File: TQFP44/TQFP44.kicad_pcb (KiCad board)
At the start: 2 copper layers, 56.1 x 20.6 mm, 12 parts, among them J1 Conn_01x22, J2 Conn_01x22, J3 Conn_02x22_Counter_Clockwise, J4 Conn_02x22_Counter_Clockwise, J5 Conn_02x22_Counter_Clockwise, J6 Conn_01x06

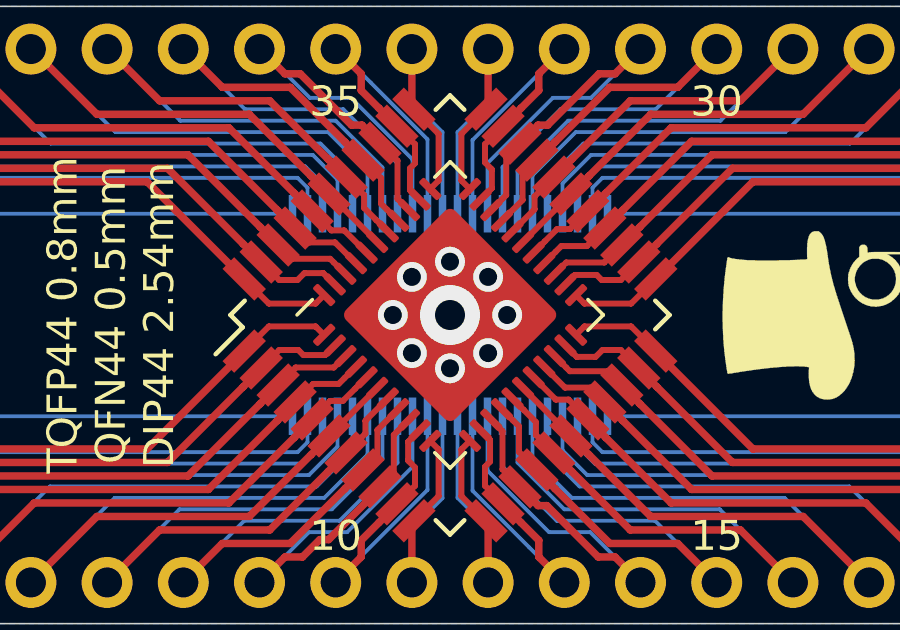
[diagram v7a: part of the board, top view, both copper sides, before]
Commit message: Silkscreen Edits
Dimensions moved to Drawings Layer
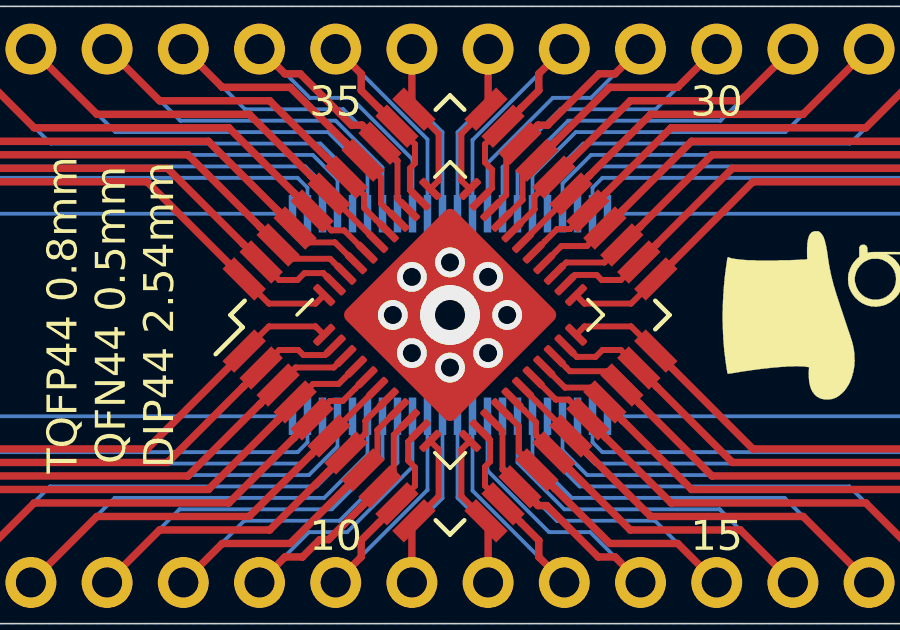
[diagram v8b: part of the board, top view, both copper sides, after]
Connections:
- J4 pad 45: (no net) -> Net-(J6-Pad1)
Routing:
- net Net-(J6-Pad1): vias 0 -> 9
- net (no net): vias 9 -> 0
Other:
- rule pad_to_mask_clearance: 0.051 -> 0
- rule solder_mask_min_width: 0.25 -> 0.1
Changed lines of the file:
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@@
   (page A4)
   (layers
-    (0 F.Cu signal)
+    (0 F.Cu signal hide)
     (31 B.Cu signal)
     (32 B.Adhes user hide)
@@
     (34 B.Paste user hide)
     (35 F.Paste user hide)
-    (36 B.SilkS user)
+    (36 B.SilkS user hide)
     (37 F.SilkS user)
     (38 B.Mask user)
-    (39 F.Mask user)
+    (39 F.Mask user hide)
     (40 Dwgs.User user)
     (41 Cmts.User user hide)
@@
     (pad_size 1.7 1.7)
     (pad_drill 1)
-    (pad_to_mask_clearance 0.051)
-    (solder_mask_min_width 0.25)
+    (pad_to_mask_clearance 0)
+    (solder_mask_min_width 0.1)
     (aux_axis_origin 0 0)
     (visible_elements 7FFFFFFF)
@@
       (usegerberadvancedattributes false)
       (creategerberjobfile false)
-      (excludeedgelayer false)
+      (excludeedgelayer true)
       (linewidth 0.100000)
       (plotframeref false)
       (viasonmask false)
       (mode 1)
-      (useauxorigin false)
+      (useauxorigin true)
       (hpglpennumber 1)
       (hpglpenspeed 20)
@@
     (pad "" smd roundrect (at -1.935 -0.645 45) (size 1.04 1.04) (layers F.Paste) (roundrect_rratio 0.240385))
     (pad "" smd roundrect (at -1.935 -1.935 45) (size 1.04 1.04) (layers F.Paste) (roundrect_rratio 0.240385))
-    (pad 45 smd roundrect (at 0 0 45) (size 5.15 5.15) (layers F.Cu F.Mask) (roundrect_rratio 0.048544))
+    (pad 45 smd roundrect (at 0 0 45) (size 5.15 5.15) (layers F.Cu F.Mask) (roundrect_rratio 0.048544)
+      (net 45 "Net-(J6-Pad1)"))
     (model ${KISYS3DMOD}/Package_DFN_QFN.3dshapes/QFN-44-1EP_7x7mm_P0.5mm_EP5.15x5.15mm.wrl
       (at (xyz 0 0 0))
@@
     (effects (font (size 1 1) (thickness 0.15)) (justify mirror))
   )
-  (dimension 56.134 (width 0.15) (layer F.SilkS)
-    (gr_text "56.134 mm" (at 194.437 56.0278) (layer F.SilkS)
+  (dimension 56.134 (width 0.15) (layer Dwgs.User)
+    (gr_text "56.134 mm" (at 194.437 56.0278) (layer Dwgs.User)
       (effects (font (size 1 1) (thickness 0.15)) hide)
     )
@@
     (arrow2b (pts (xy 166.37 57.3278) (xy 167.496504 56.741379)))
   )
-  (dimension 20.574 (width 0.15) (layer F.SilkS)
-    (gr_text "20.574 mm" (at 160.447298 72.39 270) (layer F.SilkS)
+  (dimension 20.574 (width 0.15) (layer Dwgs.User)
+    (gr_text "20.574 mm" (at 160.447298 72.39 270) (layer Dwgs.User)
       (effects (font (size 1 1) (thickness 0.15)) hide)
     )
@@
     (arrow2b (pts (xy 161.747298 62.103) (xy 162.333719 63.229504)))
   )
-  (dimension 17.78 (width 0.15) (layer F.SilkS)
-    (gr_text "17.780 mm" (at 163.5206 72.4154 270) (layer F.SilkS)
+  (dimension 17.78 (width 0.15) (layer Dwgs.User)
+    (gr_text "17.780 mm" (at 163.5206 72.4154 270) (layer Dwgs.User)
       (effects (font (size 1 1) (thickness 0.15)) hide)
     )
@@
     (arrow2b (pts (xy 164.8206 63.5254) (xy 165.407021 64.651904)))
   )
-  (dimension 53.34 (width 0.15) (layer F.SilkS)
-    (gr_text "53.340 mm" (at 194.437 58.7202) (layer F.SilkS)
+  (dimension 53.34 (width 0.15) (layer Dwgs.User)
+    (gr_text "53.340 mm" (at 194.437 58.7202) (layer Dwgs.User)
       (effects (font (size 1 1) (thickness 0.15)) hide)
     )
@@
   (gr_circle (center 195.707 73.66) (end 196.107 73.66) (layer F.Mask) (width 0.2))
   (gr_circle (center 195.715 73.66) (end 196.115 73.66) (layer B.Mask) (width 0.2))
-  (gr_circle (center 194.437 74.187) (end 194.837 74.187) (layer B.Mask) (width 0.2))
+  (gr_circle (center 194.437 74.149) (end 194.837 74.149) (layer B.Mask) (width 0.2))
   (gr_circle (center 194.437 74.168) (end 194.837 74.168) (layer F.Mask) (width 0.2))
   (gr_circle (center 193.175 73.66) (end 193.575 73.66) (layer B.Mask) (width 0.2))
@@
   (gr_line (start 166.37 63.5) (end 166.37 81.28) (layer Edge.Cuts) (width 0.05))
   (gr_line (start 221.107 62.103) (end 167.767 62.103) (layer Edge.Cuts) (width 0.05))
+  (via (at 194.437 72.39) (size 2) (drill 1) (layers F.Cu B.Cu) (net 45))
+  (via (at 192.532 72.39) (size 1) (drill 0.6) (layers F.Cu B.Cu) (net 45))
+  (via (at 196.342 72.39) (size 1) (drill 0.6) (layers F.Cu B.Cu) (net 45))
+  (via (at 194.437 70.6374) (size 1) (drill 0.6) (layers F.Cu B.Cu) (net 45))
+  (via (at 193.167 71.12) (size 1) (drill 0.6) (layers F.Cu B.Cu) (net 45))
+  (via (at 195.707 71.12) (size 1) (drill 0.6) (layers F.Cu B.Cu) (net 45))
+  (via (at 193.167 73.66) (size 1) (drill 0.6) (layers F.Cu B.Cu) (net 45))
+  (via (at 194.437 74.1426) (size 1) (drill 0.6) (layers F.Cu B.Cu) (net 45))
+  (via (at 195.707 73.66) (size 1) (drill 0.6) (layers F.Cu B.Cu) (net 45))
   (segment (start 198.635447 71.727087) (end 198.91736 72.009) (width 0.2) (layer F.Cu) (net 1))
   (segment (start 200.474854 72.009) (end 201.295936 71.187918) (width 0.2) (layer F.Cu) (net 1))
@@
   (segment (start 172.217078 76.855322) (end 184.340224 76.855322) (width 0.25) (layer F.Cu) (net 44))
   (segment (start 167.767 81.3054) (end 172.217078 76.855322) (width 0.25) (layer F.Cu) (net 44))
-  (via (at 194.437 72.39) (size 2) (drill 1) (layers F.Cu B.Cu) (net 0))
-  (via (at 192.532 72.39) (size 1) (drill 0.6) (layers F.Cu B.Cu) (net 0))
-  (via (at 196.342 72.39) (size 1) (drill 0.6) (layers F.Cu B.Cu) (net 0))
-  (via (at 194.437 70.612) (size 1) (drill 0.6) (layers F.Cu B.Cu) (net 0))
-  (via (at 193.167 71.12) (size 1) (drill 0.6) (layers F.Cu B.Cu) (net 0))
-  (via (at 195.707 71.12) (size 1) (drill 0.6) (layers F.Cu B.Cu) (net 0))
-  (via (at 193.167 73.66) (size 1) (drill 0.6) (layers F.Cu B.Cu) (net 0))
-  (via (at 194.437 74.168) (size 1) (drill 0.6) (layers F.Cu B.Cu) (net 0))
-  (via (at 195.707 73.66) (size 1) (drill 0.6) (layers F.Cu B.Cu) (net 0))
   (zone (net 45) (net_name "Net-(J6-Pad1)") (layer B.Cu) (hatch none 0.508)
     (connect_pads (clearance 0.5))
